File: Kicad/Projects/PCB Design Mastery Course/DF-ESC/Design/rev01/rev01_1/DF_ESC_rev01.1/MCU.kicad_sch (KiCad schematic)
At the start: 0 parts

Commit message: Update 5
MCU schematic wiring design
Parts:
- added C201, C202, C203, C204, C205, C206, C208, C209, C212, C213, C216, C217: 100n, symbol Device:C
- added C207, C210, C211: 10p, symbol Device:C
- added C214, C215: 2u2, symbol Device:C
- added D201: LED, symbol Device:LED
- added D202: LED_G, symbol Device:LED
- added D203: LED_R, symbol Device:LED
- added FB201: FerriteBead, symbol Device:FerriteBead
- added J201: Conn_01x06, symbol Connector_Generic:Conn_01x06
- added J202: Conn_01x03, symbol Connector_Generic:Conn_01x03
- added J203: Conn_01x08, symbol Connector_Generic:Conn_01x08
- added R201, R202, R203: 0R, symbol Device:R
- added R204, R205, R206: 1K, symbol Device:R
- added R207, R208, R210: 2k2, symbol Device:R
- added R209: 39k, symbol Device:R
- added SW201: SW_DIP_x01, symbol Switch:SW_DIP_x01
- added TH201: 10k, symbol Device:Thermistor_NTC
- added U201: STM32F405RGTx, Package_QFP:LQFP-64_10x10mm_P0.5mm, symbol MCU_ST_STM32F4:STM32F405RGTx
- added Y201: Crystal, symbol Device:Crystal
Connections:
- new net: D201.2 (A), R204.2
- new net: D203.2 (A), R206.2
- new net: C208.1, C209.1, FB201.1, U201.13 (VDDA)
- new net: C208.2, C209.2
- new net: D202.2 (A), R205.2
- new net: J202.3 (Pin_3), R207.1
- new net +3V3: C201.1, C202.1, C203.1, C204.1, C205.1, C206.1, C207.1, C216.1, FB201.2, J201.1 (Pin_1), J203.2 (Pin_2), R201.1, R204.1, TH201.1, U201.1 (VBAT), U201.19 (VDD), U201.32 (VDD), U201.48 (VDD), U201.64 (VDD)
- new net +5V: J202.1 (Pin_1), J203.1 (Pin_1)
- new net +VDC: R209.1
- new net ADC_TEMP: R208.1, TH201.2, U201.17 (PA3)
- new net AN_IN: C217.1, R209.2, R210.1, U201.10 (PC2)
- new net BOOT0_P: R201.2, U201.60 (BOOT0)
- new net BR_S01: U201.27 (PB1)
- new net BR_S02: U201.26 (PB0)
- new net CAN_RX: U201.61 (PB8)
- new net CAN_TX: U201.62 (PB9)
- new net DC_CAL: U201.33 (PB12)
- new net EN_GATE: U201.51 (PC10)
- new net FAULT: U201.53 (PC12)
- new net GND: C201.2, C202.2, C203.2, C204.2, C205.2, C206.2, C207.2, C210.2, C211.2, C212.2, C213.2, C214.2, C215.2, C216.2, C217.2, D201.1 (K), D202.1 (K), D203.1 (K), J201.3 (Pin_3), J202.2 (Pin_2), J203.3 (Pin_3), J203.8 (Pin_8), R208.2, R210.2, SW201.1, U201.12 (VSSA), U201.18 (VSS), U201.63 (VSS)
- new net H1: U201.43 (PA10)
- new net H2: U201.42 (PA9)
- new net H3: U201.41 (PA8)
- new net HALL_1: U201.58 (PB6)
- new net HALL_2: U201.59 (PB7)
- new net HALL_3: U201.52 (PC11)
- new net L1: U201.36 (PB15)
- new net L2: U201.35 (PB14)
- new net L3: U201.34 (PB13)
- new net LED_GREEN: R205.1, U201.24 (PC4)
- new net LED_RED: R206.1, U201.25 (PC5)
- new net MISO_ADC_EXT2: J203.7 (Pin_7), U201.22 (PA6)
- new net NRST: C213.1, J201.5 (Pin_5), SW201.2, U201.7 (NRST)
- new net PH0: C210.1, R202.1, Y201.2
- new net PH1: C211.1, R203.1, Y201.1
- new net PH_0_P: R202.2, U201.5 (PH0)
- new net PH_1_P: R203.2, U201.6 (PH1)
- new net RX_SCL_MOSI: J203.6 (Pin_6), U201.23 (PA7), U201.29 (PB10), U201.38 (PC7)
- new net SCK_ADC_EXT: J203.4 (Pin_4), U201.21 (PA5)
- new net SENS1: U201.16 (PA2)
- new net SENS2: U201.15 (PA1)
- new net SENS3: U201.14 (PA0)
- new net SERVO: C212.1, R207.2, U201.57 (PB5)
- new net SWDIO: J201.4 (Pin_4), U201.46 (PA13)
- new net SWLCK: J201.2 (Pin_2), U201.49 (PA14)
- new net TEMP_MOTOR: U201.8 (PC0)
- new net TX_SDA_NSS: J203.5 (Pin_5), U201.20 (PA4), U201.30 (PB11), U201.37 (PC6)
- new net USB_DM: U201.44 (PA11)
- new net USB_DP: U201.45 (PA12)
- new net VCAP_1: C214.1, U201.31 (VCAP_1)
- new net VCAP_2: C215.1, U201.47 (VCAP_2)
- no-connect marks 0 -> 13
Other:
- note added: "COMMUNICATION PROTOCOL"
- note added: "Decoupling capacitors. Put one as close as possible to VDD pin."
- note added: "MCU"
- note added: "NRST internally pulled-up"
- note added: "NTC THERMISTOR"
- note added: "PROGRAMMING / DEBUG"
- note added: "SERVO"
- note added: "SUBTITUDE WITH 100R IF USED AS SERVO OUTPUT"
- note added: "See Boot Modes Table 7"
- note added: "VOLTAGE DIVIDER"
- note added: "WHEN: VDC=60V=>AN_IN=3V204"

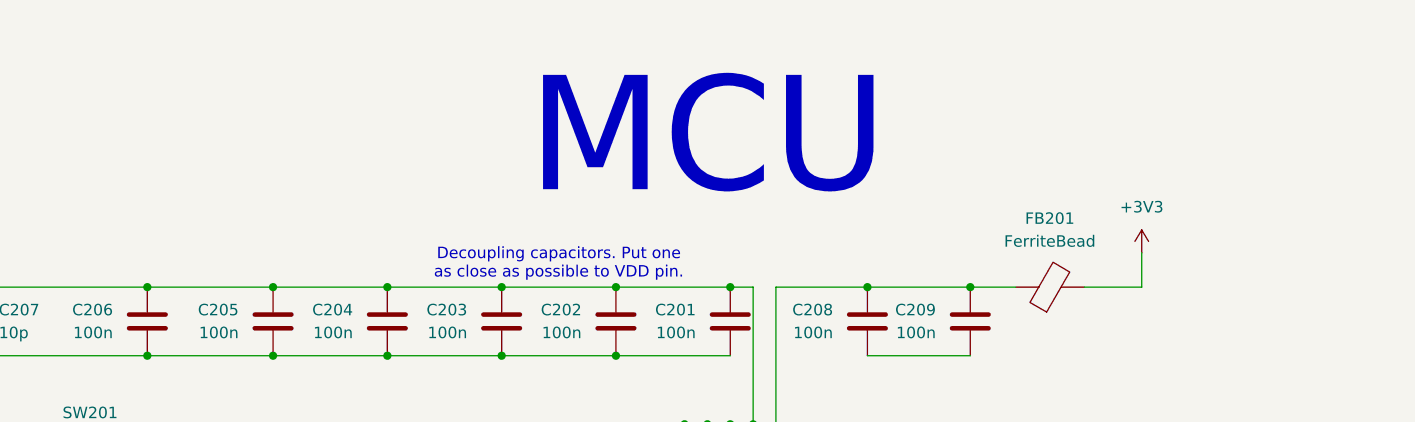
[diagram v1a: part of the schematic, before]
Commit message: Update 7
Completed MOSFET_DRIVER Schematic
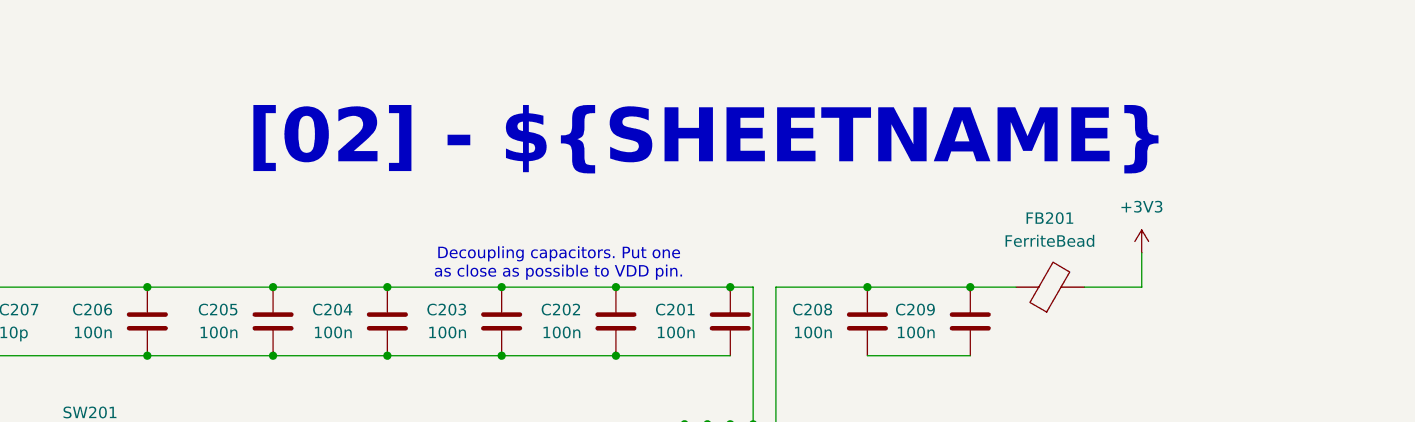
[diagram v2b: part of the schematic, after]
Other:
- note added: "[02] - ${SHEETNAME}"
- note removed: "MCU"
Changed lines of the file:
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@@
 		)
 	)
-	(text "MCU"
+	(text "[02] - ${SHEETNAME}"
 		(exclude_from_sim no)
 		(at 139.7 26.67 0)
 		(effects
 			(font
-				(size 12.7 12.7)
-				(thickness 1.5875)
+				(size 6 6)
+				(thickness 1.2)
+				(bold yes)
 			)
 		)
